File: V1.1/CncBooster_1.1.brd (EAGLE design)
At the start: 98 parts, among them IC1 FT230XS, IC2 LM2596S, J1 J1, J10 PDI, J14 TTL Serial, J2 J2, J3 J3, J4 J4, J5 J5, J6 J6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

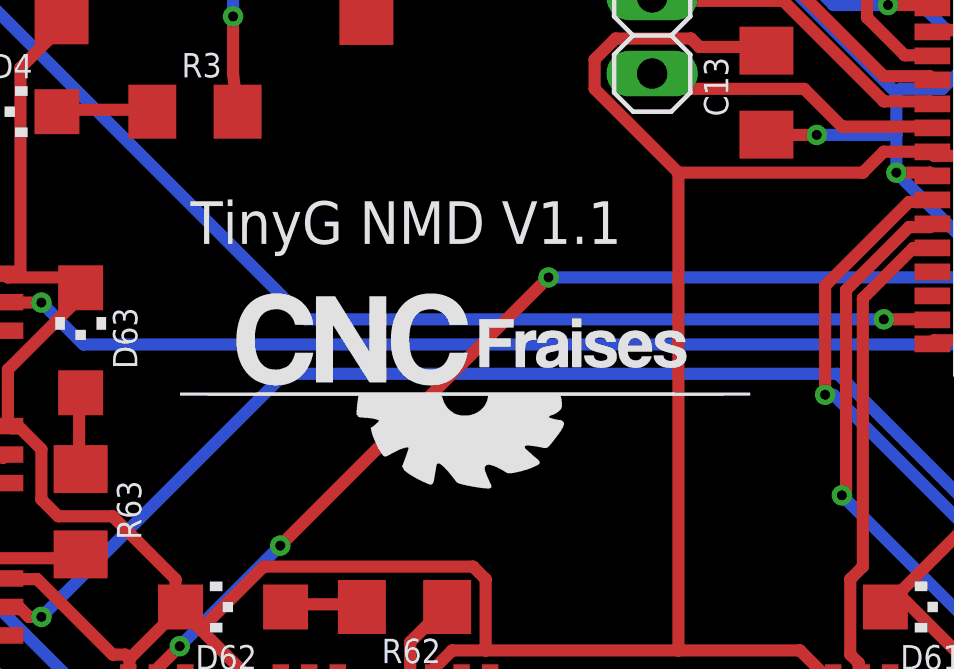
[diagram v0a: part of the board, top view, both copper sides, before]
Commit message: Modification du nom de la carte sur le PCB
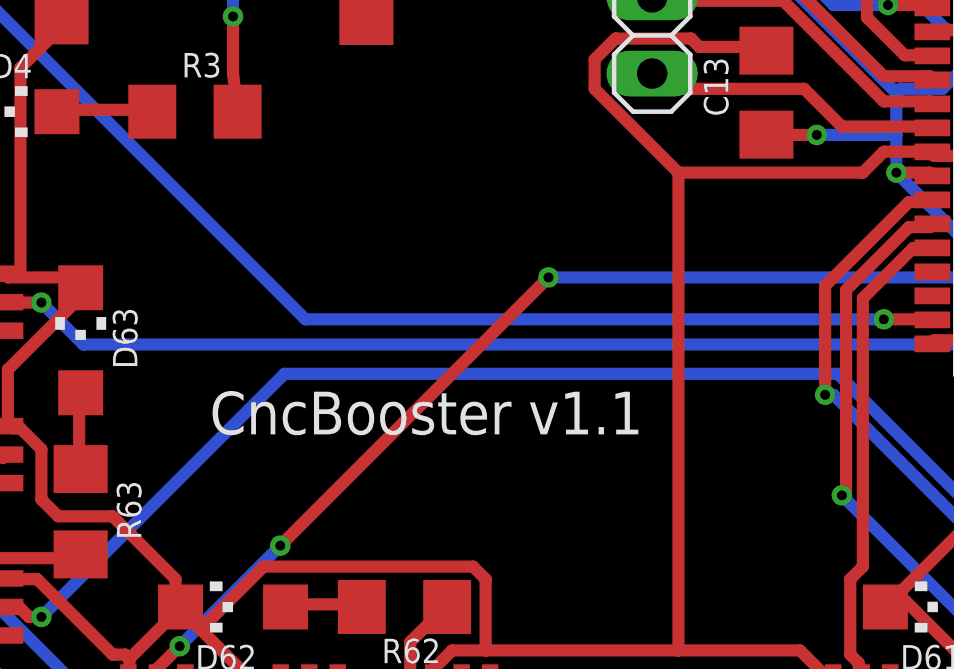
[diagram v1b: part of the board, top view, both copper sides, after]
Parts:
- removed U$3: (no value), Logo_Cncfraises:LOGO_CNCFRAISES_0.4
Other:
- board text added: "CncBooster v1.1"
- board text removed: "TinyG NMD V1.1"
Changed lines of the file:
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@@
 <text x="10.3433" y="76.3425" size="0.8128" layer="25" font="vector" ratio="11" rot="SR270">+Vmot</text>
 <text x="11.6133" y="74.4377" size="0.8128" layer="25" font="vector" ratio="11" rot="SR270">30V max</text>
-<text x="22.714" y="31.152625" size="1.4224" layer="21" font="vector" ratio="17">TinyG NMD V1.1</text>
+<text x="23.349" y="24.802625" size="1.4224" layer="21" font="vector" ratio="17">CncBooster v1.1</text>
 </plain>
 <attributes>
@@
 <attribute name="VALUE" x="61.595" y="48.895" size="1.27" layer="27" rot="R180"/>
 </element>
-<element name="U$3" library="Logo_Cncfraises" package="LOGO_CNCFRAISES_0.4" value="" x="22.225" y="22.86"/>
 </elements>
 <signals>
